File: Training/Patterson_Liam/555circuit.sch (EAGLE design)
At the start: 7 parts, among them IC1 LM555D

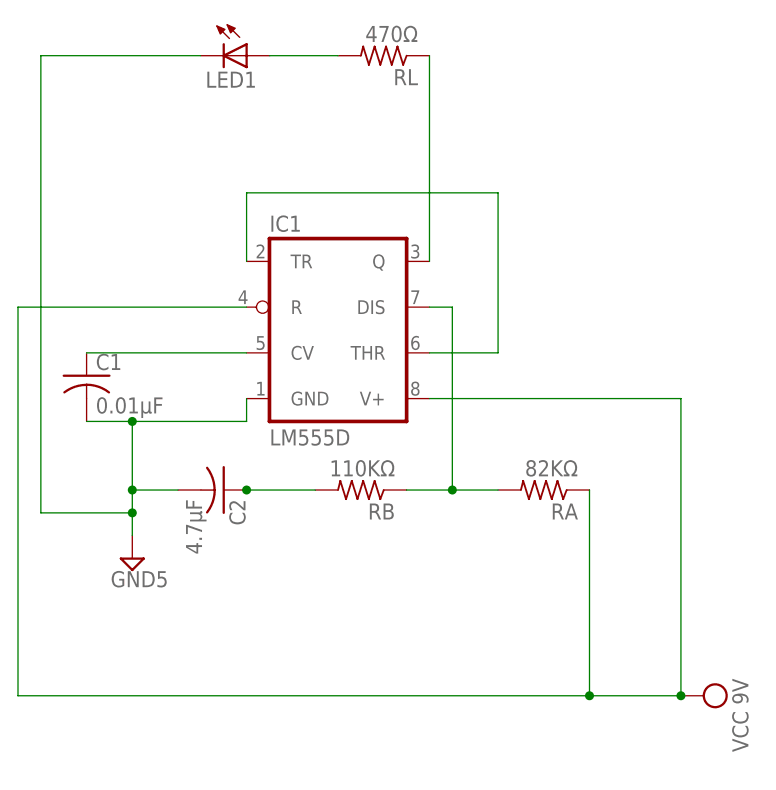
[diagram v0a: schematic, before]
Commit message: ERC ran without error, fixed threshold pin.
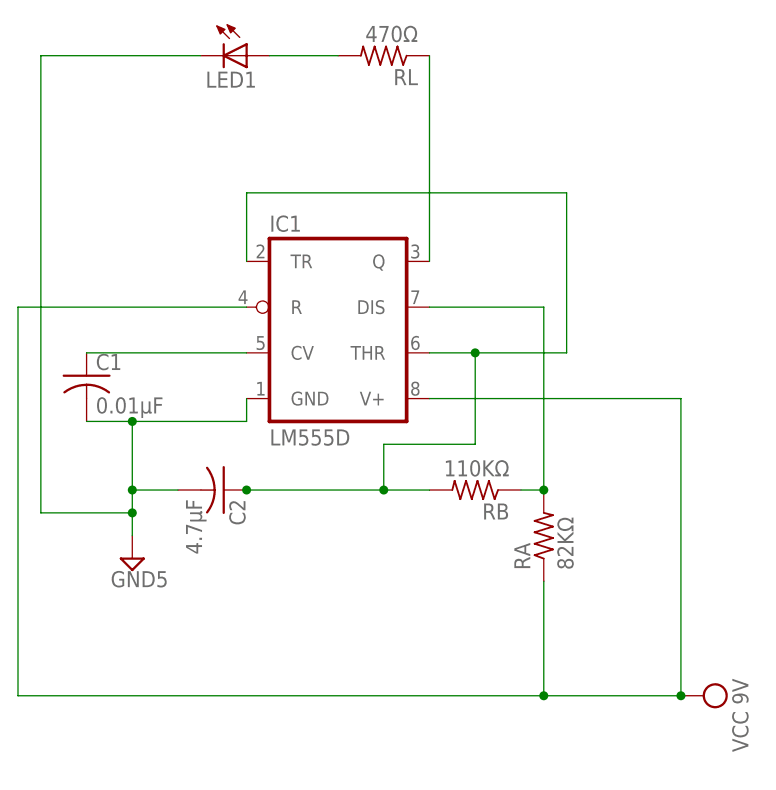
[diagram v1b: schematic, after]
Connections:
- removed net N$3: C2.1, RB.2
- net N$1: now also C2.1, RB.2
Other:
- moved on the sheet: RA, RB
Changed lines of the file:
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@@
 <instance part="SUPPLY1" gate="G$1" x="43.18" y="43.18"/>
 <instance part="C1" gate="G$1" x="38.1" y="63.5"/>
-<instance part="RB" gate="G$1" x="68.58" y="50.8" rot="R180"/>
-<instance part="RA" gate="G$1" x="88.9" y="50.8" rot="R180"/>
+<instance part="RB" gate="G$1" x="81.28" y="50.8" rot="R180"/>
+<instance part="RA" gate="G$1" x="88.9" y="45.72" rot="R90"/>
 <instance part="LED1" gate="G$1" x="55.88" y="99.06" rot="R270"/>
 <instance part="C2" gate="G$1" x="53.34" y="50.8" rot="R270"/>
@@
 <wire x1="55.88" y1="71.12" x2="30.48" y2="71.12" width="0.1524" layer="91"/>
 <wire x1="30.48" y1="71.12" x2="30.48" y2="27.94" width="0.1524" layer="91"/>
-<wire x1="30.48" y1="27.94" x2="93.98" y2="27.94" width="0.1524" layer="91"/>
+<wire x1="30.48" y1="27.94" x2="88.9" y2="27.94" width="0.1524" layer="91"/>
 <pinref part="IC1" gate="A" pin="V+"/>
 <junction x="104.14" y="27.94"/>
-<wire x1="93.98" y1="27.94" x2="104.14" y2="27.94" width="0.1524" layer="91"/>
+<wire x1="88.9" y1="27.94" x2="104.14" y2="27.94" width="0.1524" layer="91"/>
 <wire x1="76.2" y1="60.96" x2="104.14" y2="60.96" width="0.1524" layer="91"/>
 <wire x1="104.14" y1="60.96" x2="104.14" y2="27.94" width="0.1524" layer="91"/>
 <pinref part="RA" gate="G$1" pin="1"/>
-<wire x1="93.98" y1="50.8" x2="93.98" y2="27.94" width="0.1524" layer="91"/>
-<junction x="93.98" y="27.94"/>
+<wire x1="88.9" y1="40.64" x2="88.9" y2="27.94" width="0.1524" layer="91"/>
+<junction x="88.9" y="27.94"/>
 </segment>
 </net>
@@
 <pinref part="RB" gate="G$1" pin="1"/>
 <pinref part="RA" gate="G$1" pin="2"/>
-<wire x1="83.82" y1="50.8" x2="78.74" y2="50.8" width="0.1524" layer="91"/>
-<wire x1="78.74" y1="50.8" x2="73.66" y2="50.8" width="0.1524" layer="91"/>
-<wire x1="78.74" y1="71.12" x2="78.74" y2="50.8" width="0.1524" layer="91"/>
-<junction x="78.74" y="50.8"/>
+<wire x1="88.9" y1="71.12" x2="88.9" y2="50.8" width="0.1524" layer="91"/>
+<junction x="88.9" y="50.8"/>
 <pinref part="IC1" gate="A" pin="DIS"/>
-<wire x1="76.2" y1="71.12" x2="78.74" y2="71.12" width="0.1524" layer="91"/>
+<wire x1="76.2" y1="71.12" x2="88.9" y2="71.12" width="0.1524" layer="91"/>
+<wire x1="88.9" y1="50.8" x2="86.36" y2="50.8" width="0.1524" layer="91"/>
 </segment>
 </net>
@@
 <wire x1="66.04" y1="99.06" x2="58.42" y2="99.06" width="0.1524" layer="91"/>
 <pinref part="LED1" gate="G$1" pin="A"/>
-</segment>
-</net>
-<net name="N$3" class="0">
-<segment>
-<pinref part="RB" gate="G$1" pin="2"/>
-<pinref part="C2" gate="G$1" pin="1"/>
-<wire x1="55.88" y1="50.8" x2="63.5" y2="50.8" width="0.1524" layer="91"/>
-<junction x="55.88" y="50.8"/>
 </segment>
 </net>
@@
 <pinref part="IC1" gate="A" pin="TR"/>
 <wire x1="55.88" y1="76.2" x2="55.88" y2="83.82" width="0.1524" layer="91"/>
-<wire x1="55.88" y1="83.82" x2="83.82" y2="83.82" width="0.1524" layer="91"/>
-<wire x1="83.82" y1="83.82" x2="83.82" y2="66.04" width="0.1524" layer="91"/>
+<wire x1="55.88" y1="83.82" x2="91.44" y2="83.82" width="0.1524" layer="91"/>
+<wire x1="91.44" y1="83.82" x2="91.44" y2="66.04" width="0.1524" layer="91"/>
 <pinref part="IC1" gate="A" pin="THR"/>
-<wire x1="83.82" y1="66.04" x2="76.2" y2="66.04" width="0.1524" layer="91"/>
+<wire x1="91.44" y1="66.04" x2="81.28" y2="66.04" width="0.1524" layer="91"/>
+<wire x1="81.28" y1="66.04" x2="76.2" y2="66.04" width="0.1524" layer="91"/>
+<wire x1="81.28" y1="66.04" x2="81.28" y2="55.88" width="0.1524" layer="91"/>
+<junction x="81.28" y="66.04"/>
+<wire x1="81.28" y1="55.88" x2="71.12" y2="55.88" width="0.1524" layer="91"/>
+<pinref part="RB" gate="G$1" pin="2"/>
+<pinref part="C2" gate="G$1" pin="1"/>
+<wire x1="55.88" y1="50.8" x2="71.12" y2="50.8" width="0.1524" layer="91"/>
+<junction x="55.88" y="50.8"/>
+<wire x1="71.12" y1="50.8" x2="76.2" y2="50.8" width="0.1524" layer="91"/>
+<wire x1="71.12" y1="55.88" x2="71.12" y2="50.8" width="0.1524" layer="91"/>
+<junction x="71.12" y="50.8"/>
 </segment>
 </net>
